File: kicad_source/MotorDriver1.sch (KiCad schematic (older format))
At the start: 25 parts, among them CN10 CONN_01X04, CN11 CONN_01X05, U2 TMC5130A-TA

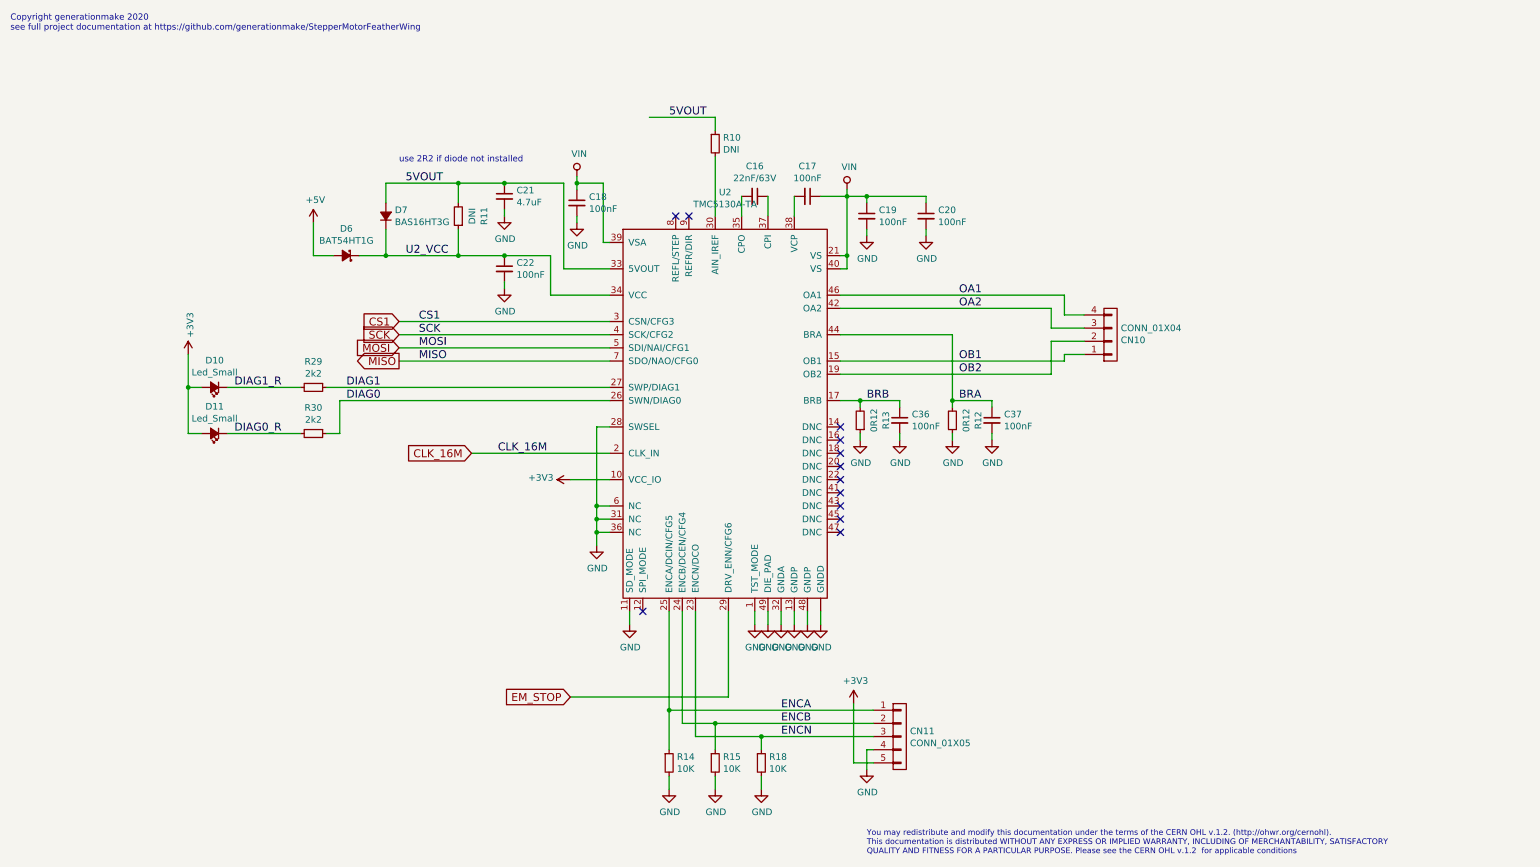
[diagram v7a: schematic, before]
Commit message: updated part numbers
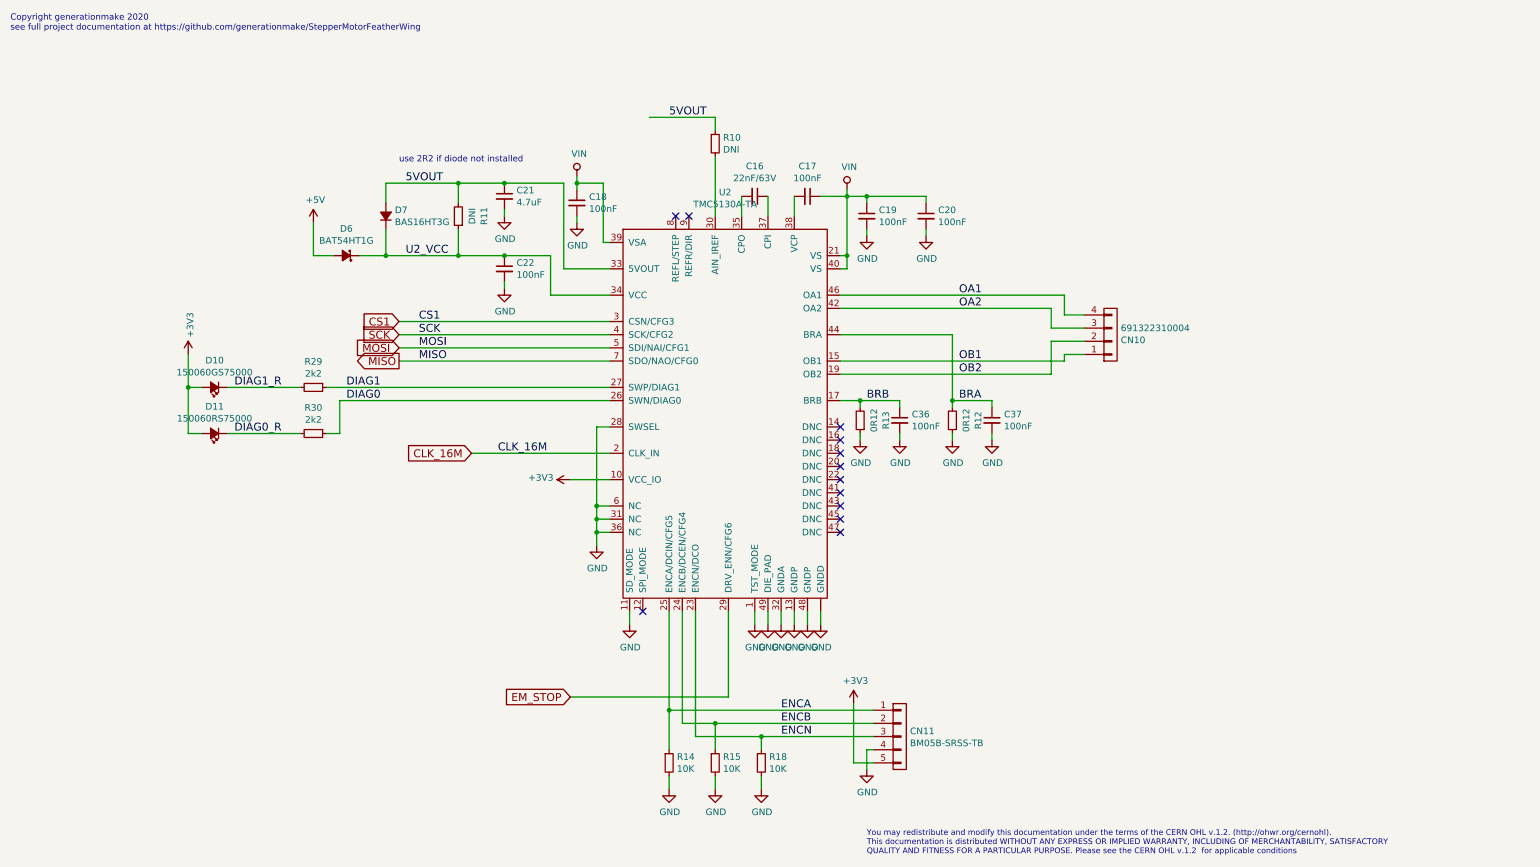
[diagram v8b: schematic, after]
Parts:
- CN10: value CONN_01X04 -> 691322310004
- CN11: value CONN_01X05 -> BM05B-SRSS-TB
- D10: value Led_Small -> 150060GS75000
- D11: value Led_Small -> 150060RS75000
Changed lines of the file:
@@
 P 8850 2950
 F 0 "CN10" H 8928 2991 50  0000 L CNN
-F 1 "CONN_01X04" H 8928 2900 50  0000 L CNN
+F 1 "691322310004" H 8928 2900 50  0000 L CNN
 F 2 "CON_wuerth:WR-TBL_691322310004" H 8850 2950 50  0001 C CNN
 F 3 "" H 8850 2950 50  0000 C CNN
@@
 P 7250 6000
 F 0 "CN11" H 7328 6041 50  0000 L CNN
-F 1 "CONN_01X05" H 7328 5950 50  0000 L CNN
+F 1 "BM05B-SRSS-TB" H 7328 5950 50  0000 L CNN
 F 2 "connectors_JST_SH:Connectors_JST_BM05B-SRSS-TB" H 7250 6000 50  0001 C CNN
 F 3 "" H 7250 6000 50  0000 C CNN
@@
 P 2050 3350
 F 0 "D10" H 2050 3145 50  0000 C CNN
-F 1 "Led_Small" H 2050 3236 50  0000 C CNN
+F 1 "150060GS75000" H 2050 3236 50  0000 C CNN
 F 2 "LEDs:LED_0603" V 2050 3350 50  0001 C CNN
 F 3 "" V 2050 3350 50  0000 C CNN
@@
 P 2050 3700
 F 0 "D11" H 2050 3495 50  0000 C CNN
-F 1 "Led_Small" H 2050 3586 50  0000 C CNN
+F 1 "150060RS75000" H 2050 3586 50  0000 C CNN
 F 2 "LEDs:LED_0603" V 2050 3700 50  0001 C CNN
 F 3 "" V 2050 3700 50  0000 C CNN
